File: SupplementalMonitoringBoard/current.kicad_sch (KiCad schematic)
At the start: 7 parts, among them U2 OPA842xDBV

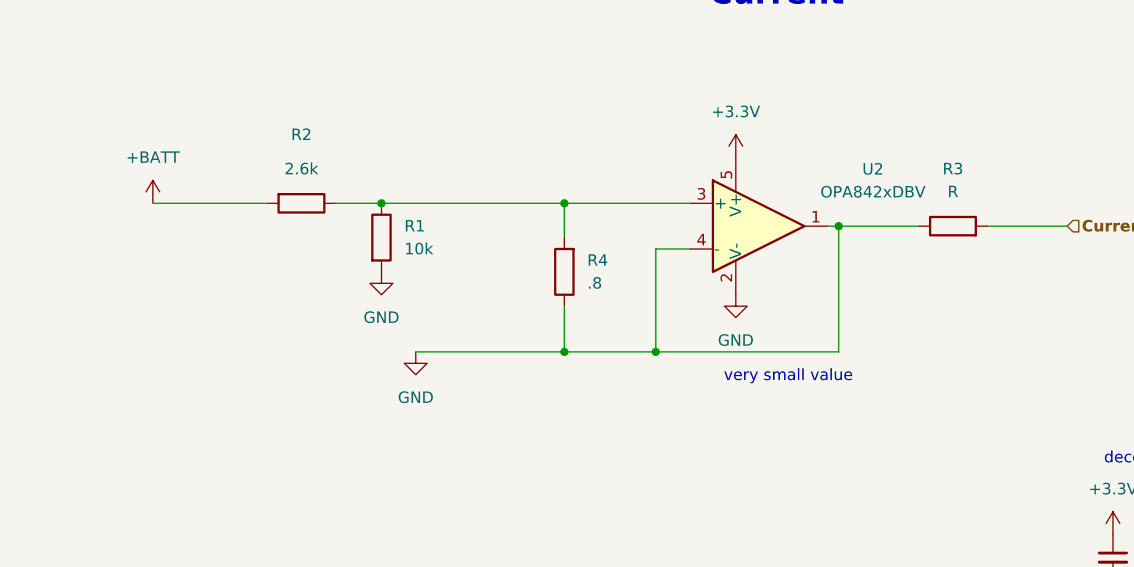
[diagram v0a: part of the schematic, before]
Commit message: Supplemental Monitoring Board Changes
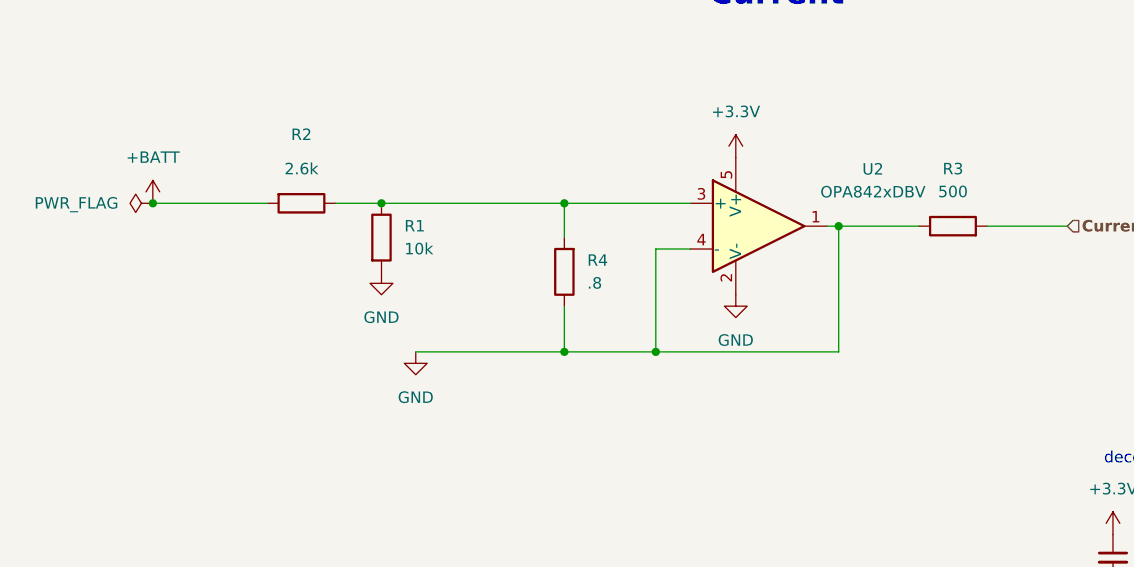
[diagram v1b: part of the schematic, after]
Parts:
- R3: value R -> 500
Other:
- note removed: "very small value"
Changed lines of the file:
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@@
+		(color 0 0 0 0)
+	)
+	(junction
+		(at 73.66 90.17)
+		(diameter 0)
 		(color 0 0 0 0)
 	)
@@
 				(size 1.27 1.27)
 				(thickness 0.1588)
-			)
-		)
-	)
-	(text "very small value\n"
-		(exclude_from_sim no)
-		(at 144.272 109.474 0)
-		(effects
-			(font
-				(size 1.27 1.27)
 			)
 		)
@@
 			)
 		)
-		(property "Value" "R"
+		(property "Value" "500"
 			(at 162.56 88.9 90)
 			(effects
@@
 					(unit 1)
 				)
+			)
+		)
+	)
+	(symbol
+		(lib_id "power:PWR_FLAG")
+		(at 73.66 90.17 90)
+		(unit 1)
+		(exclude_from_sim no)
+		(in_bom yes)
+		(on_board yes)
+		(dnp no)
+		(fields_autoplaced yes)
+		(property "Reference" "#FLG02"
+			(at 71.755 90.17 0)
+			(effects
+				(font
+					(size 1.27 1.27)
+				)
+				(hide yes)
+			)
+		)
+		(property "Value" "PWR_FLAG"
+			(at 69.85 90.1699 90)
+			(effects
+				(font
+					(size 1.27 1.27)
+				)
+				(justify left)
+			)
+		)
+		(property "Footprint" ""
+			(at 73.66 90.17 0)
+			(effects
+				(font
+					(size 1.27 1.27)
+				)
+				(hide yes)
+			)
+		)
+		(property "Datasheet" "~"
+			(at 73.66 90.17 0)
+			(effects
+				(font
+					(size 1.27 1.27)
+				)
+				(hide yes)
+			)
+		)
+		(property "Description" "Special symbol for telling ERC where power comes from"
+			(at 73.66 90.17 0)
+			(effects
+				(font
+					(size 1.27 1.27)
+				)
+				(hide yes)
+			)
+		)
+		(pin "1"
+		)
+		(instances
+			(project ""
+				(path "/aa0415d0-3287-4bc4-9a8e-766ada9ace2f/1e74c2bc-637a-422a-831e-fab1291cbb0a"
+					(reference "#FLG02")
+					(unit 1)
+				)

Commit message: thing
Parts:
- added R14: 100, Resistor_SMD:R_0805_2012Metric, symbol Device:R
- C1, C2: footprint (none) -> Capacitor_SMD:C_0805_2012Metric
- R1: footprint (none) -> Resistor_SMD:R_0805_2012Metric
- R2: value 2.6k -> 30k; footprint (none) -> Resistor_SMD:R_0805_2012Metric
- R3: value 500 -> 8; footprint (none) -> Resistor_SMD:R_0805_2012Metric
- R4: value .8 -> 100k; footprint (none) -> Resistor_SMD:R_0805_2012Metric
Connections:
- net GND: now also R14.1; no longer R3.1, R4.1, U2.1, U2.4 (-)
- net at R1.1, R2.1, U2.3 (+): no longer R4.2
- new net: R3.1, R4.2, U2.1
- new net: R14.2, R4.1, U2.4 (-)
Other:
- moved on the sheet: R1, R2

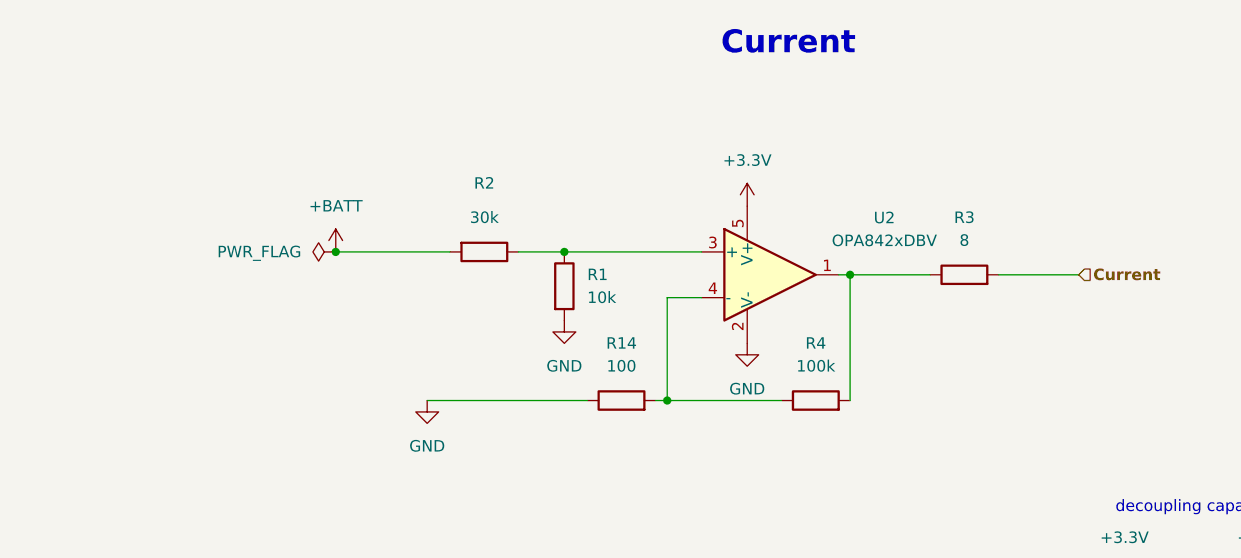
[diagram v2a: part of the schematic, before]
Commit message: Supplemental Monitoring Board
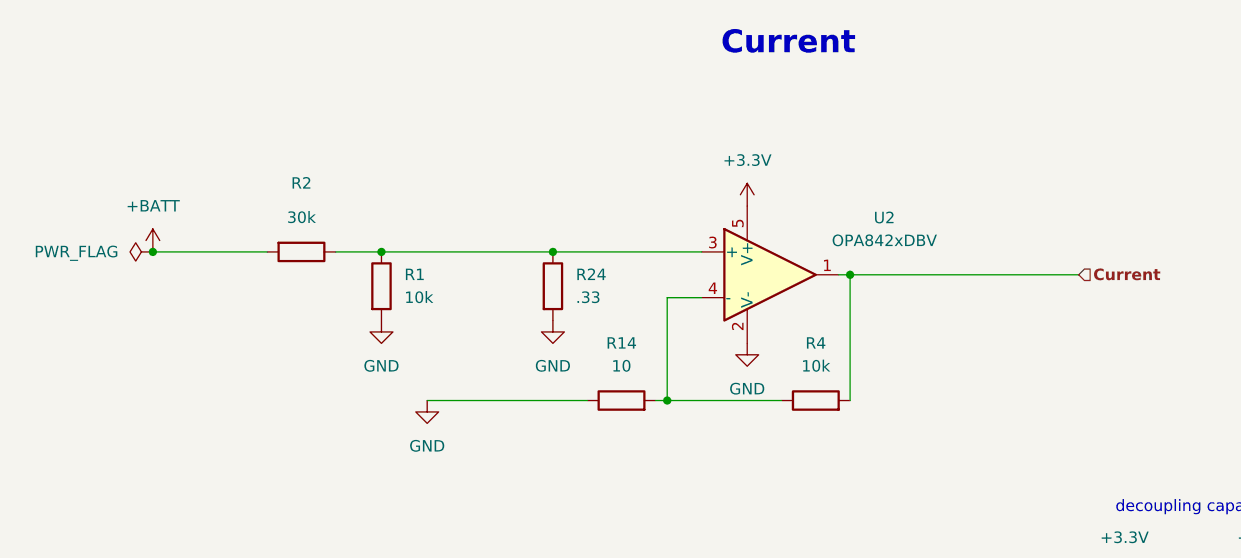
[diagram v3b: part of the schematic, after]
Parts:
- removed R3: 8, Resistor_SMD:R_0805_2012Metric, symbol Device:R
- added R24: .33, Resistor_SMD:R_0805_2012Metric, symbol Device:R
- R14: value 100 -> 10
- R4: value 100k -> 10k
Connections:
- net Current: now also R4.2, U2.1
- net GND: now also R24.2
- net at R1.1, R2.1, U2.3 (+): now also R24.1
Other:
- moved on the sheet: R1, R2

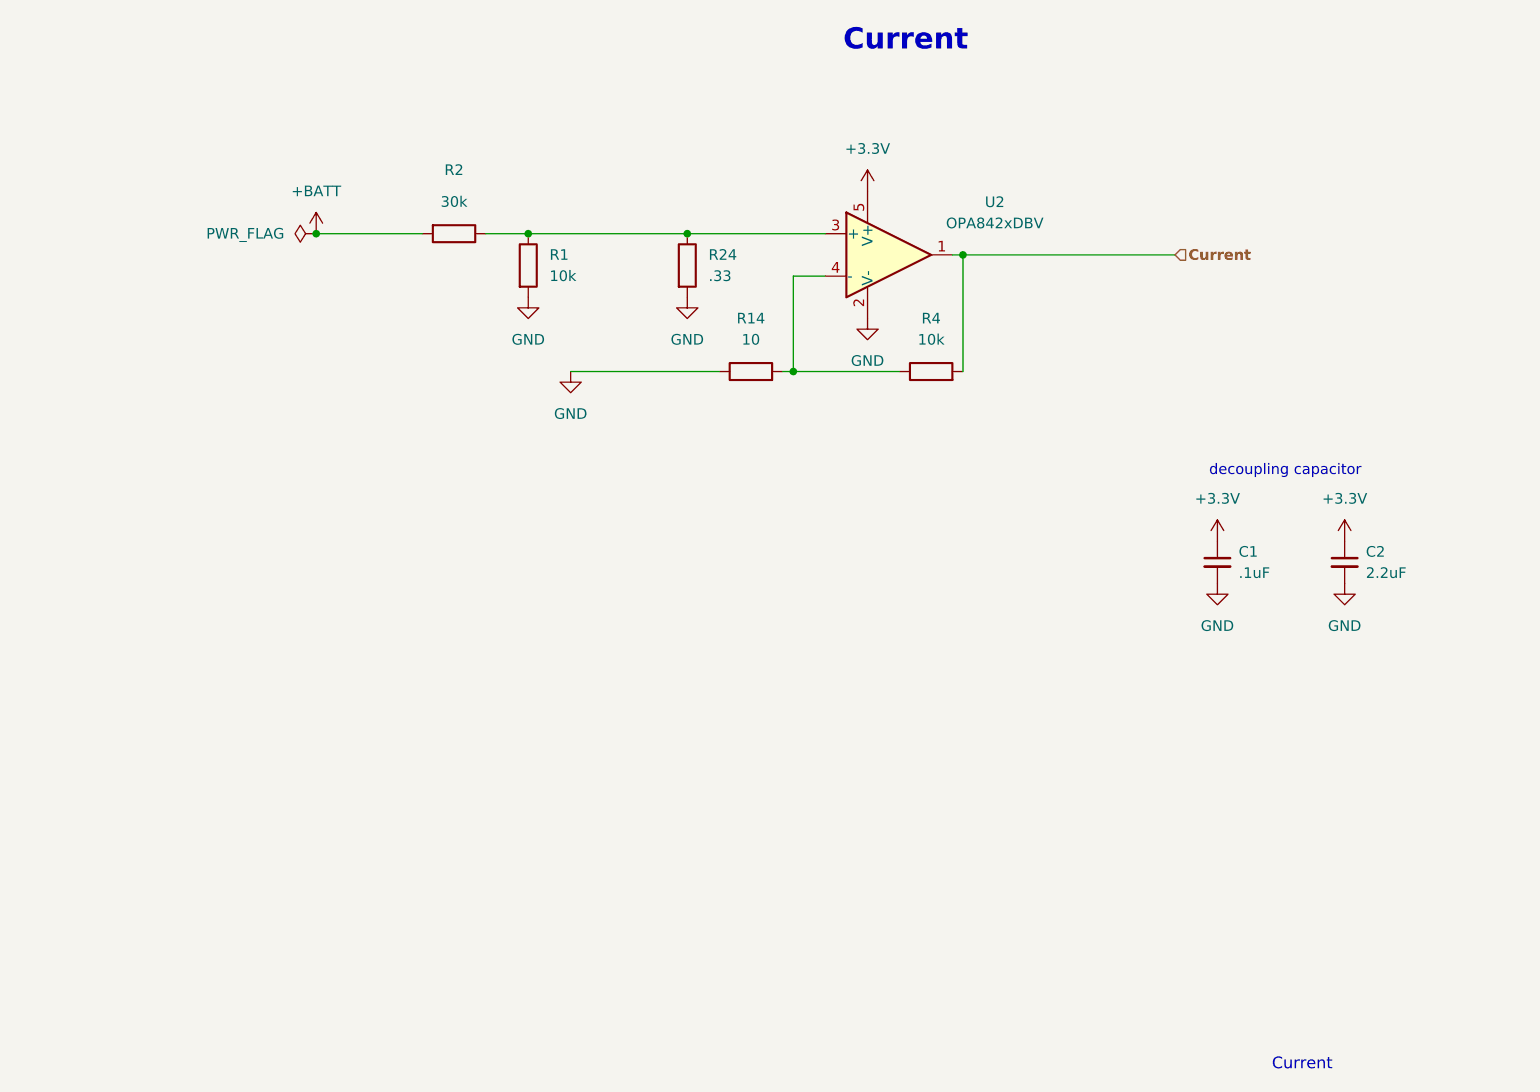
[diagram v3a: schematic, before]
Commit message: Adressed Reviews - Supplemental Monitoring Board
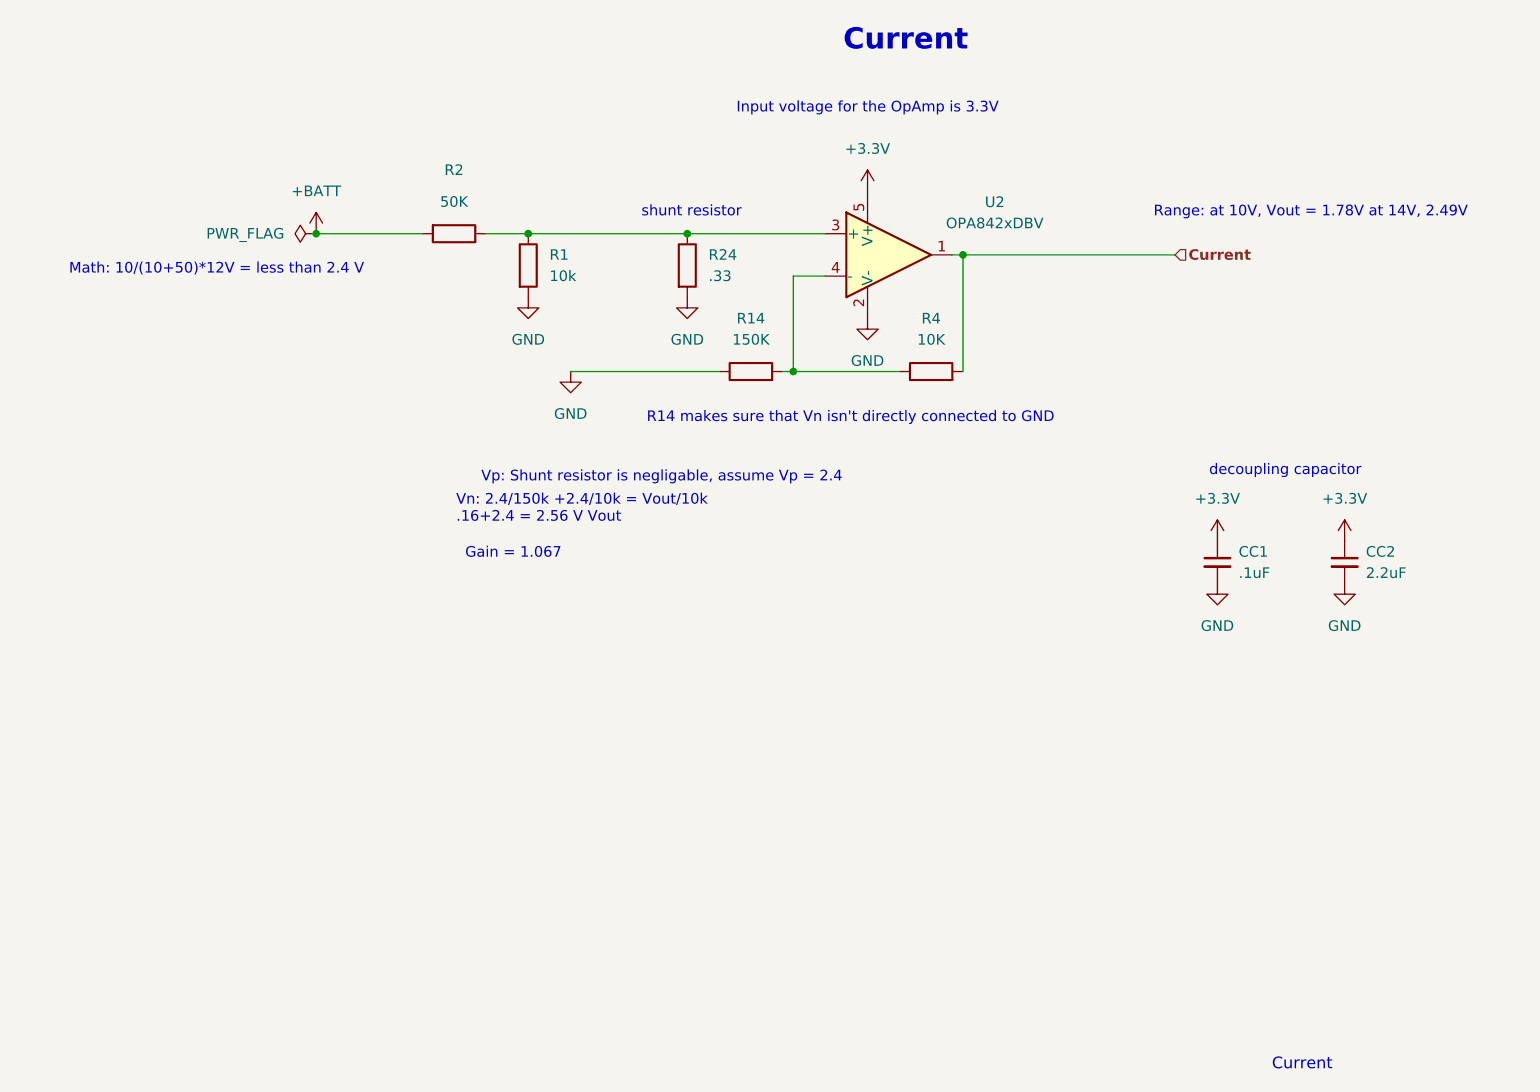
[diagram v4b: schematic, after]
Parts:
- R14: value 10 -> 150K
- R2: value 30k -> 50K
- R4: value 10k -> 10K
- renumbered C1 to CC1, C2 to CC2
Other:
- note added: "Gain = 1.067"
- note added: "Input voltage for the OpAmp is 3.3V"
- note added: "Math: 10/(10+50)*12V = less than 2.4 V"
- note added: "R14 makes sure that Vn isn't directly connected to GND"
- note added: "Range: at 10V, Vout = 1.78V at 14V, 2.49V"
- note added: "Vn: 2.4/150k +2.4/10k = Vout/10k .16+2.4 = 2.56 V Vout"
- note added: "Vp: Shunt resistor is negligable, assume Vp = 2.4"
- note added: "shunt resistor"
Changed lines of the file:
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@@
+		)
+	)
+	(text "shunt resistor\n"
+		(exclude_from_sim no)
+		(at 117.348 87.63 0)
+		(effects
+			(font
+				(size 1.27 1.27)
+			)
+		)
+	)
+	(text "Vn: 2.4/150k +2.4/10k = Vout/10k\n.16+2.4 = 2.56 V Vout\n"
+		(exclude_from_sim no)
+		(at 89.154 123.19 0)
+		(effects
+			(font
+				(size 1.27 1.27)
+			)
+			(justify left)
+		)
+	)
+	(text "Input voltage for the OpAmp is 3.3V\n"
+		(exclude_from_sim no)
+		(at 138.43 75.184 0)
+		(effects
+			(font
+				(size 1.27 1.27)
+			)
+		)
+	)
+	(text "Math: 10/(10+50)*12V = less than 2.4 V"
+		(exclude_from_sim no)
+		(at 60.452 94.488 0)
+		(effects
+			(font
+				(size 1.27 1.27)
+			)
+		)
+	)
+	(text "Gain = 1.067"
+		(exclude_from_sim no)
+		(at 96.012 128.524 0)
+		(effects
+			(font
+				(size 1.27 1.27)
+			)
 		)
 	)
@@
 				(size 1.27 1.27)
 				(thickness 0.1588)
+			)
+		)
+	)
+	(text "Vp: Shunt resistor is negligable, assume Vp = 2.4\n"
+		(exclude_from_sim no)
+		(at 113.792 119.38 0)
+		(effects
+			(font
+				(size 1.27 1.27)
+			)
+		)
+	)
+	(text "R14 makes sure that Vn isn't directly connected to GND\n"
+		(exclude_from_sim no)
+		(at 136.398 112.268 0)
+		(effects
+			(font
+				(size 1.27 1.27)
 			)
 		)
@@
 		)
 	)
+	(text "Range: at 10V, Vout = 1.78V at 14V, 2.49V"
+		(exclude_from_sim no)
+		(at 191.516 87.63 0)
+		(effects
+			(font
+				(size 1.27 1.27)
+			)
+		)
+	)
 	(hierarchical_label "Current"
 		(shape input)
@@
 		(dnp no)
 		(fields_autoplaced yes)
-		(property "Reference" "C2"
+		(property "Reference" "CC2"
 			(at 198.12 128.2762 0)
 			(effects
@@
 			(project "SupplementalMonitoringBoard"
 				(path "/aa0415d0-3287-4bc4-9a8e-766ada9ace2f/1e74c2bc-637a-422a-831e-fab1291cbb0a"
-					(reference "C2")
+					(reference "CC2")
 					(unit 1)
 				)
@@
 			)
 		)
-		(property "Value" "10"
+		(property "Value" "150K"
 			(at 124.46 102.87 90)
 			(effects
@@
 		(dnp no)
 		(fields_autoplaced yes)
-		(property "Reference" "C1"
+		(property "Reference" "CC1"
 			(at 182.88 128.2762 0)
 			(effects
@@
 			(project "SupplementalMonitoringBoard"
 				(path "/aa0415d0-3287-4bc4-9a8e-766ada9ace2f/1e74c2bc-637a-422a-831e-fab1291cbb0a"
-					(reference "C1")
+					(reference "CC1")
 					(unit 1)
 				)
@@
 			)
 		)
-		(property "Value" "10k"
+		(property "Value" "10K"
 			(at 146.05 102.87 90)
 			(effects
@@
 			)
 		)
-		(property "Value" "30k"
+		(property "Value" "50K"
 			(at 88.9 86.36 90)
 			(effects
